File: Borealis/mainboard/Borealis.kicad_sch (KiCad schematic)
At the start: 21 parts, among them J1 Conn_01x03_Pin (power & reset), J2 Conn_01x03_Pin (data connecti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, J3 Conn_01x06_Pin (microSD reade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, J4 Conn_02x04_Counter_Clockwise 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, J5 Conn_01x03_Pin (power connect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, J6 MSD-1-A, SW1 Reset push button, SW3 Experiment on/off switch, U1 Pico, U2 DS3231SN#T&R

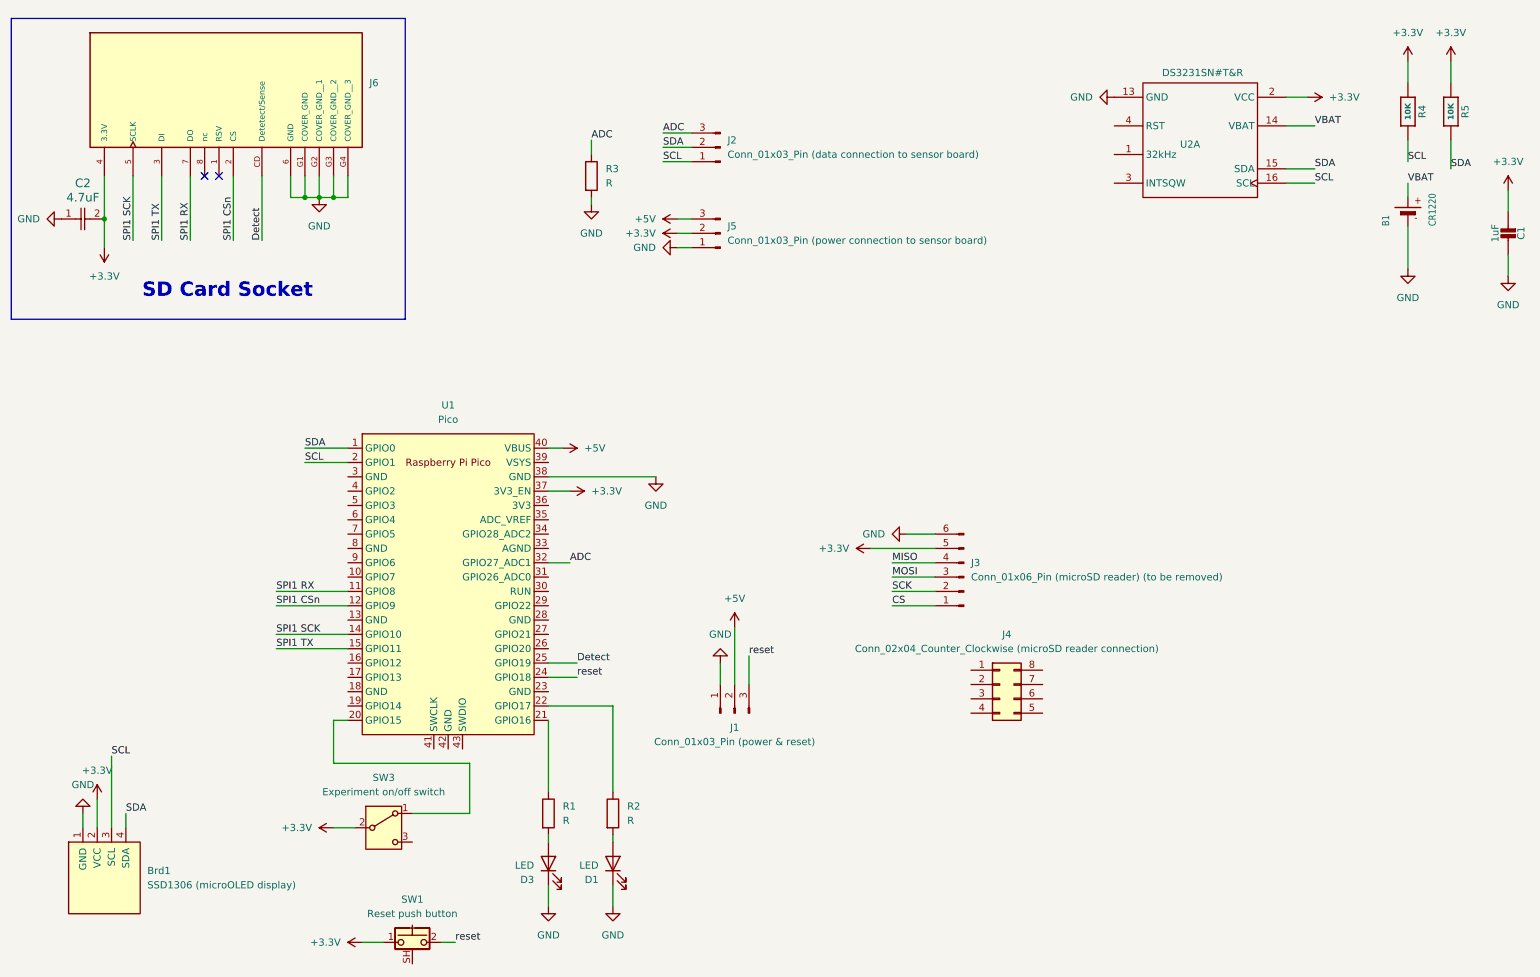
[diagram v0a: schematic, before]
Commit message: Added mainboard and temerature board
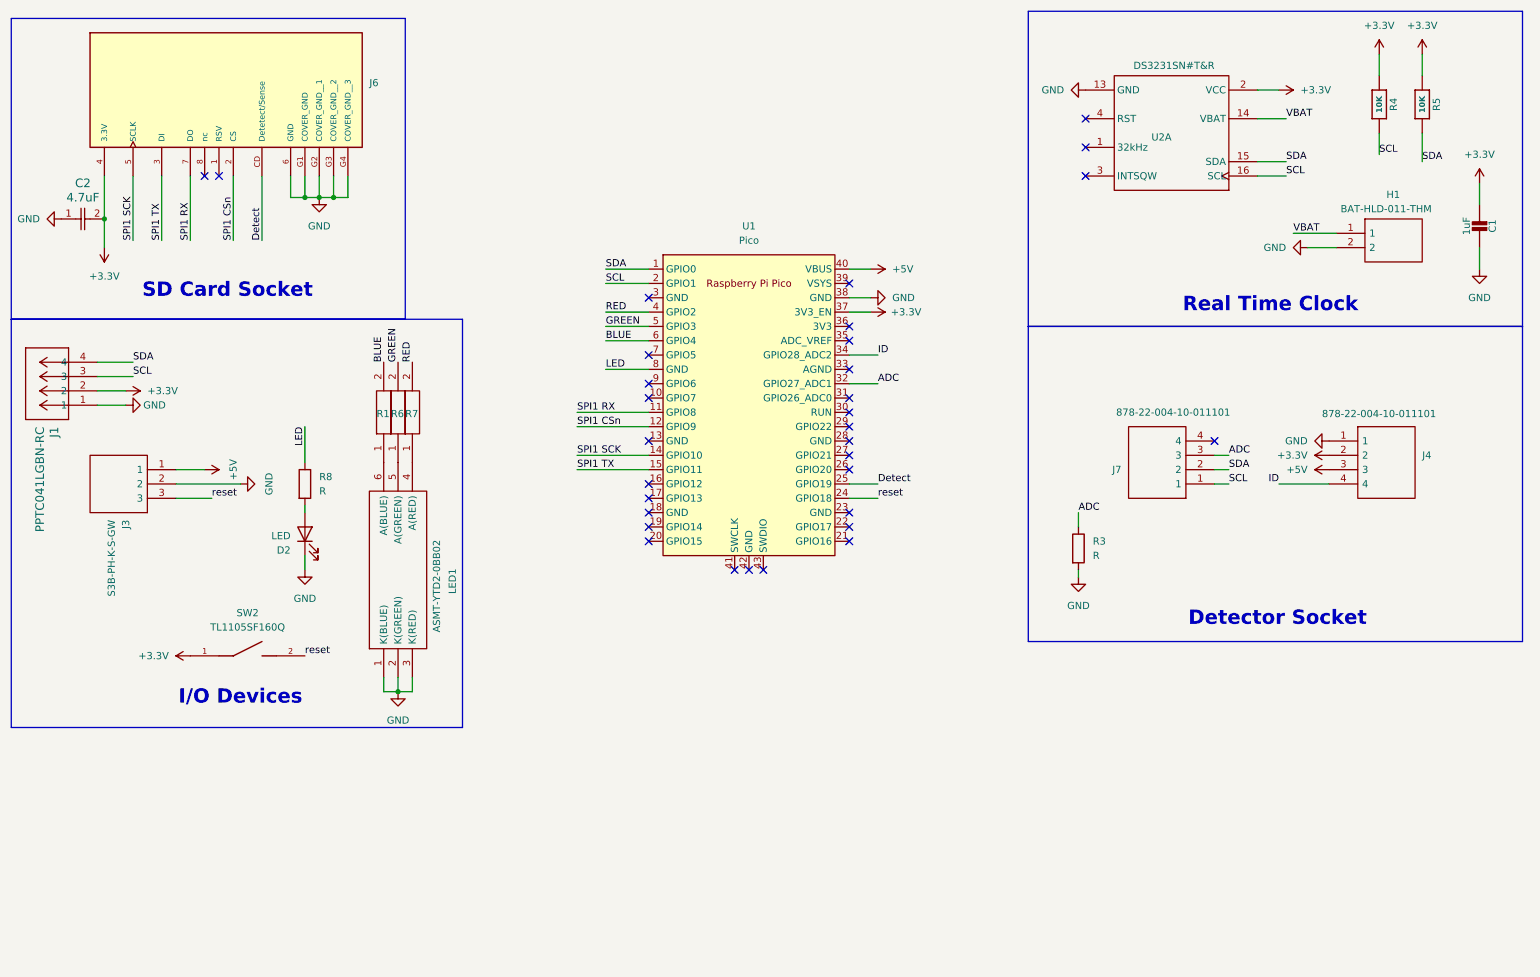
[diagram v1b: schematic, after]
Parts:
- removed B1: CR1220, batteryholder:BAT-SMD_CR1220-2, symbol Adafruit DS3231 RTC Breakout-eagle-import:BATTERYCR1220_SMT
- removed Brd1: SSD1306 (microOLED display), TG9541:Display_128x64_096_I2C, symbol SSD1306-128x64_OLED:SSD1306
- removed D1, D3: LED, LED_THT:LED_D5.0mm, symbol Device:LED
- removed J1: Conn_01x03_Pin (power & reset), batteryholder:1x03 2.3 pitch, symbol Connector:Conn_01x03_Pin
- removed J2: Conn_01x03_Pin (data connection to sensor board), batteryholder:1x03 2.3 pitch, symbol Connector:Conn_01x03_Pin
- removed J3: Conn_01x06_Pin (microSD reader) (to be removed), symbol Connector:Conn_01x06_Pin
- removed J4: Conn_02x04_Counter_Clockwise (microSD reader conn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, symbol Connector_Generic:Conn_02x04_Counter_Clockwise
- removed J5: Conn_01x03_Pin (power connection to sensor board), symbol Connector:Conn_01x03_Pin
- removed R1, R2: R, Resistor_SMD:R_0805_2012Metric, symbol Device:R
- removed SW1: Reset push button, symbol Switch:SW_Push_Shielded
- removed SW3: Experiment on/off switch, Connector_PinHeader_2.54mm:PinHeader_1x03_P2.54mm_Vertical, symbol Switch:SW_SPDT
- added D2: LED, LED_THT:LED_D5.0mm, symbol Device:LED
- added H1: BAT-HLD-011-THM, BOREALIS:BATHLD011THM, symbol BAT-HLD-011-THM:BAT-HLD-011-THM
- added J1: PPTC041LGBN-RC, BOREALIS:CONN_PPTC041LGBN-RC_SUL, symbol 2026-01-17_05-32-59:PPTC041LGBN-RC
- added J3: S3B-PH-K-S-GW, BOREALIS:S3BPHKSGW, symbol S3B-PH-K-S-GW:S3B-PH-K-S-GW
- added J4, J7: 878-22-004-10-011101, BOREALIS:8782200410011101, symbol 878-22-004-10-011101:878-22-004-10-011101
- added LED1: ASMT-YTD2-0BB02, BOREALIS:ASMTYTD20BB02, symbol ASMT-YTD2-0BB02:ASMT-YTD2-0BB02
- added R1, R6, R7: MCU08050C3300FP500, BOREALIS:RESC2012X55N, symbol MCU08050C3300FP500:MCU08050C3300FP500
- added R8: R, Resistor_SMD:R_0805_2012Metric, symbol Device:R
- added SW2: TL1105SF160Q, BOREALIS:SW_TL1105SF160Q, symbol TL1105SF160Q:TL1105SF160Q
- C1: footprint Adafruit DS3231 RTC Breakout:0805-NO -> BOREALIS:CAPC1608X90N
- C2: footprint footprints:CAP_GRM21_2p15X1p4X1p4_MUR -> BOREALIS:CAPC1608X90N
- J6: footprint MSD-1-A:CUI_MSD-1-A -> BOREALIS:CUI_MSD-1-A
- U1: footprint Module:RaspberryPi_Pico_Common_THT -> Module:RaspberryPi_Pico_Common_SMD
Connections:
- net +3.3V: now also J1.2, J4.2, SW2.1
- net +5V: now also J3.1, J4.3
- net ADC: now also J7.3
- net GND: now also D2.1 (K), H1.2, J1.1, J3.2, J4.1, LED1.1 (K(BLUE)), LED1.2 (K(GREEN)), LED1.3 (K(RED))
- net SCL: now also J1.3, J7.1
- net SDA: now also J1.4, J7.2
- net VBAT: now also H1.1
- net reset: now also J3.3, SW2.2
- net ID: now reaches U1.34 (GPIO28_ADC2)
- net ID: now also J4.4
- net RED: now reaches U1.4 (GPIO2)
- net RED: now also R7.2
- net GREEN: now reaches U1.5 (GPIO3)
- net GREEN: now also R6.2
- net BLUE: now reaches U1.6 (GPIO4)
- net BLUE: now also R1.2
- net LED: now reaches U1.8 (GND)
- net LED: now also R8.1
- new net: D2.2 (A), R8.2
- new net: LED1.6 (A(BLUE)), R1.1
- new net: LED1.4 (A(RED)), R7.1
- new net: LED1.5 (A(GREEN)), R6.1
- no-connect marks 2 -> 32
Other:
- note added: "Detector Socket"
- note added: "I/O Devices"
- note added: "Real Time Clock"
- moved on the sheet: C1, R3, R4, R5, U1, U2A
